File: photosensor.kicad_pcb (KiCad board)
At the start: 2 copper layers, 61 x 45.7 mm, 2 parts, among them P1 TSL1406R, T1 5PIN

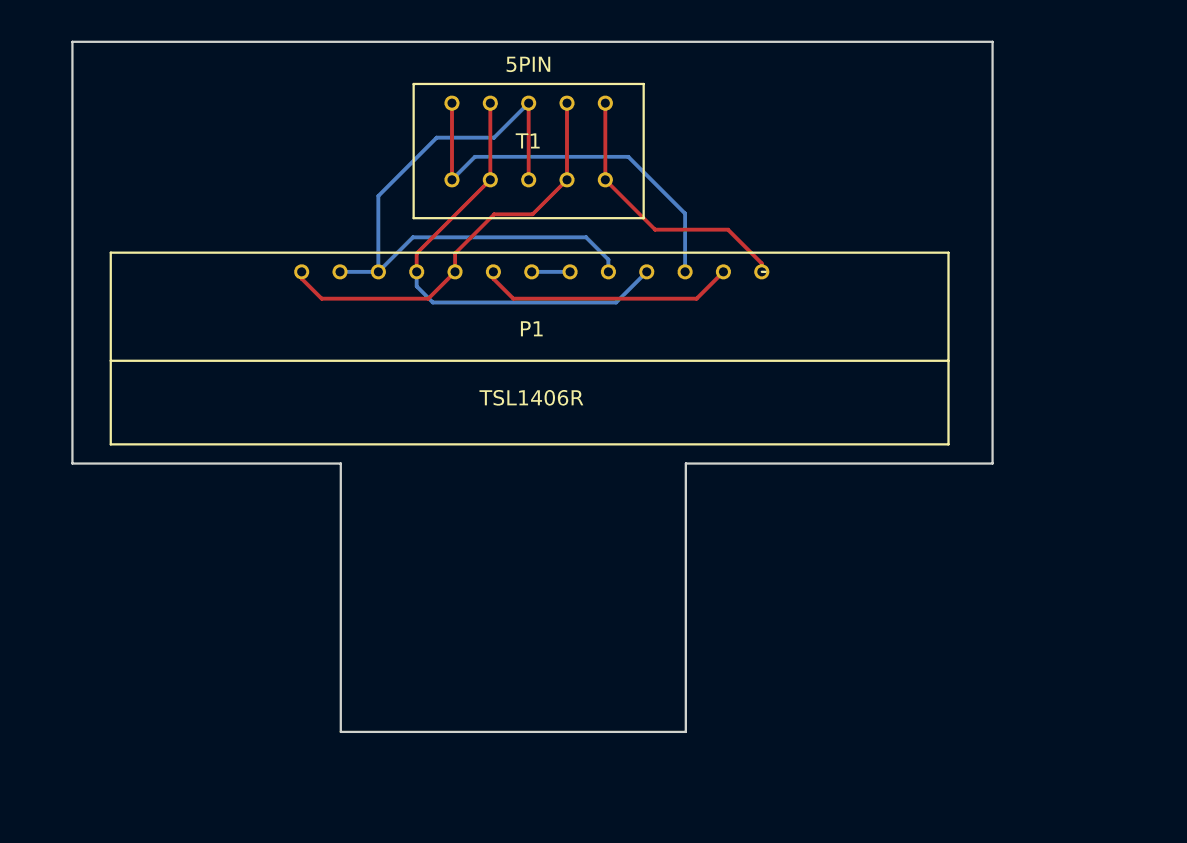
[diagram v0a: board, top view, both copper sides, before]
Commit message: change to TSL1406R
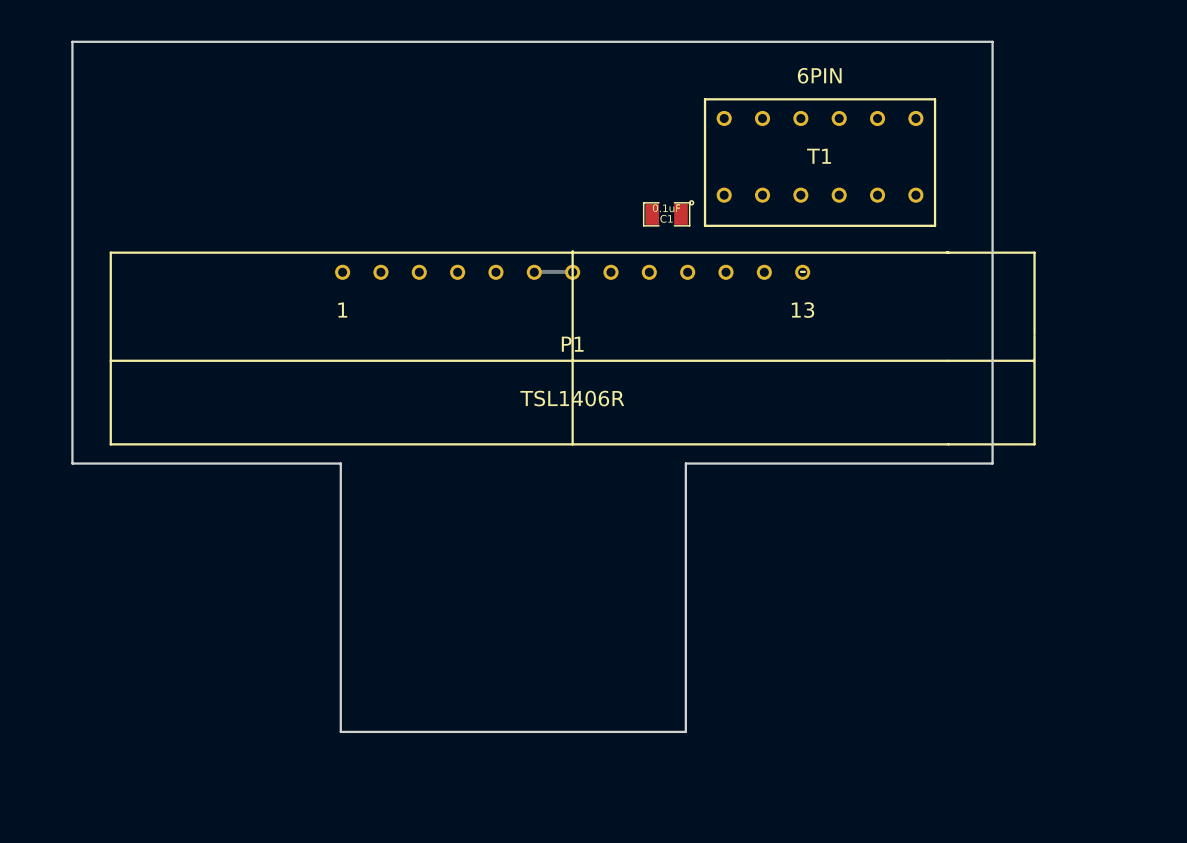
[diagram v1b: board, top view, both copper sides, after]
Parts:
- added C1: 0.1uF, SM0805, F.Cu at (222.2, 113.0)
- P1: footprint TSL1406RS -> TSL1406R
- T1: value 5PIN -> 6PIN; footprint 5Pin -> 6Pin
- moved T1 14.3 mm to (232.4, 106.7)
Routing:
- net N-000005: track 42.8 -> 0.00 mm
- net N-000003: track 30.7 -> 0.00 mm
- net GND: track 27.6 -> 0.00 mm
- net N-000001: track 26.6 -> 0.00 mm
- net +5V: track 18.3 -> 0.00 mm
- net N-000002: track 17.0 -> 2.54 mm
- net N-000004: track 2.54 -> 0.00 mm

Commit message: layout
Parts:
- added ?: , 3mm_drill_hole, F.Cu at (189.5, 121.2)
- added ?: , 3mm_drill_hole, F.Cu at (242.6, 122.7)
- moved ? 6.41 mm to (234.9, 112.6), turned to 0 degrees
- moved ? 2.41 mm to (224.6, 112.5), turned to 270 degrees
- renumbered T1 to ?, C1 to ?, P1 to ?
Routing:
- net N-000003: track 0.00 -> 71.7 mm
- net GND: track 0.00 -> 39.3 mm
- net N-000005: track 0.00 -> 38.9 mm
- net N-000002: track 2.54 -> 37.3 mm
- net N-000001: track 0.00 -> 24.3 mm
- net +5V: track 0.00 -> 23.2 mm
- net N-000004: track 0.00 -> 2.54 mm
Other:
- board size 61 x 45.7 mm -> 66 x 43.6 mm
- board text added: "AO"
- board text added: "CLK"
- board text added: "GND"
- board text added: "REV A"
- board text added: "SI"
- board text added: "SO"
- board text added: "TSL1406R Spectrophotometer Mounting"
- board text added: "Vcc"

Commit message: board outline
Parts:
- added ?: , 3mm_drill_hole, F.Cu at (208.0, 133.2)
- added ?: , 3mm_drill_hole, F.Cu at (224.0, 133.2)
- added ?: , 8mm_drill_hole, F.Cu at (216.0, 137.7)
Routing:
- net GND: track 39.3 -> 48.3 mm
- net +5V: track 23.2 -> 14.7 mm
- added copper zone on B.Cu, net +5V
- added copper zone on F.Cu, net GND
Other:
- board size 66 x 43.6 mm -> 66 x 47.1 mm

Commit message: gerber files
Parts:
- ?: value 0.1uF -> 104
- ? (x2): footprint 3mm_drill_hole -> 2.3mm_drill_hole
- moved ? 2.54 mm to (244.6, 121.2)
- moved ? 2.02 mm to (187.5, 121.2)
- moved ? 0.56 mm to (224.9, 113.0), turned to 180 degrees
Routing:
- net GND: track 48.3 -> 44.3 mm
- net +5V: track 14.7 -> 13.4 mm
- added copper zone on B.Cu, net GND
- removed copper zone on B.Cu, net +5V
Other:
- outline, holes or cut-outs redrawn
- board text added: "6PIN"
